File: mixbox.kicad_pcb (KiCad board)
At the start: 2 copper layers, 98.9 x 53.4 mm, 24 parts, among them J1 Conn_01x05_Male, J2 Conn_01x06_Male, SW1 SW_Push, SW2 SW_Push, SW3 SW_Push, SW4 SW_Push, SW5 SW_Push, SW6 SW_Push, SW7 SW_Push, SW8 SW_Push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

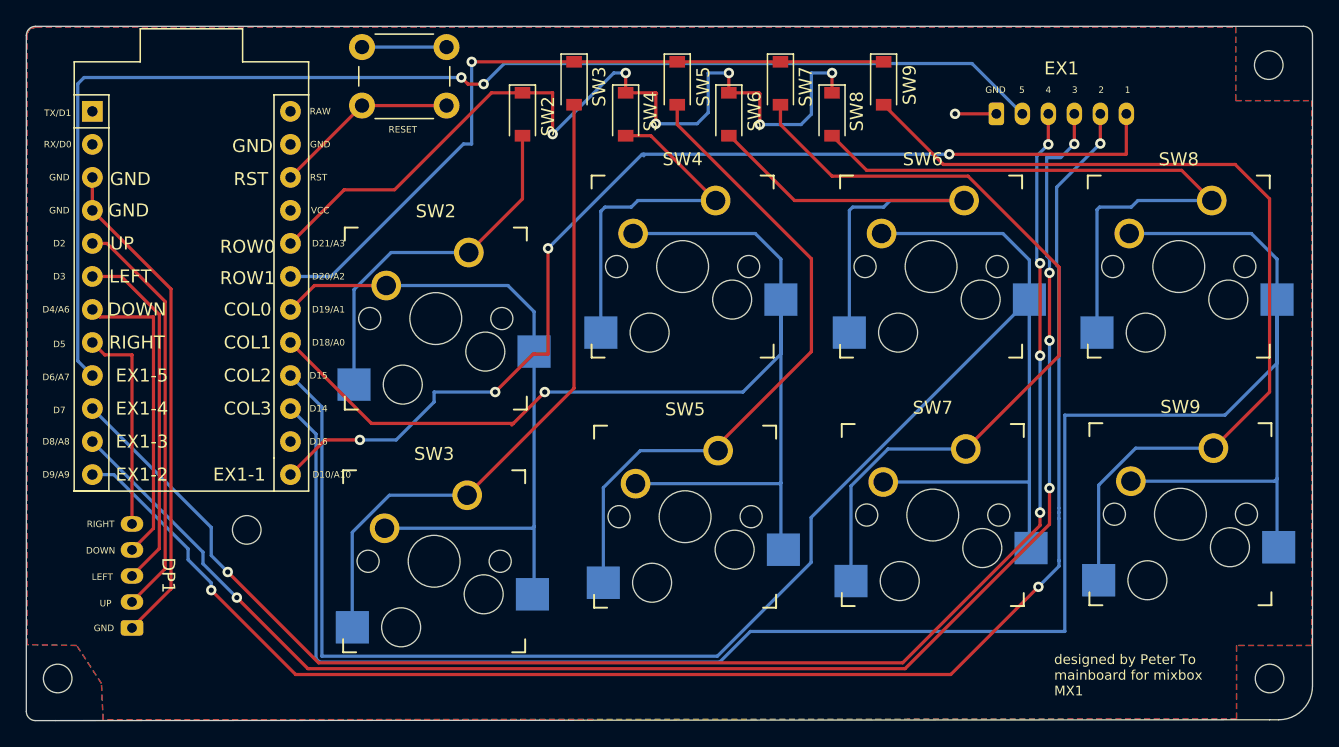
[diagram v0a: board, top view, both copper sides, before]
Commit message: Updates rows and columns in pcbnew and updates J2 from 1x06 to 1x05 connector
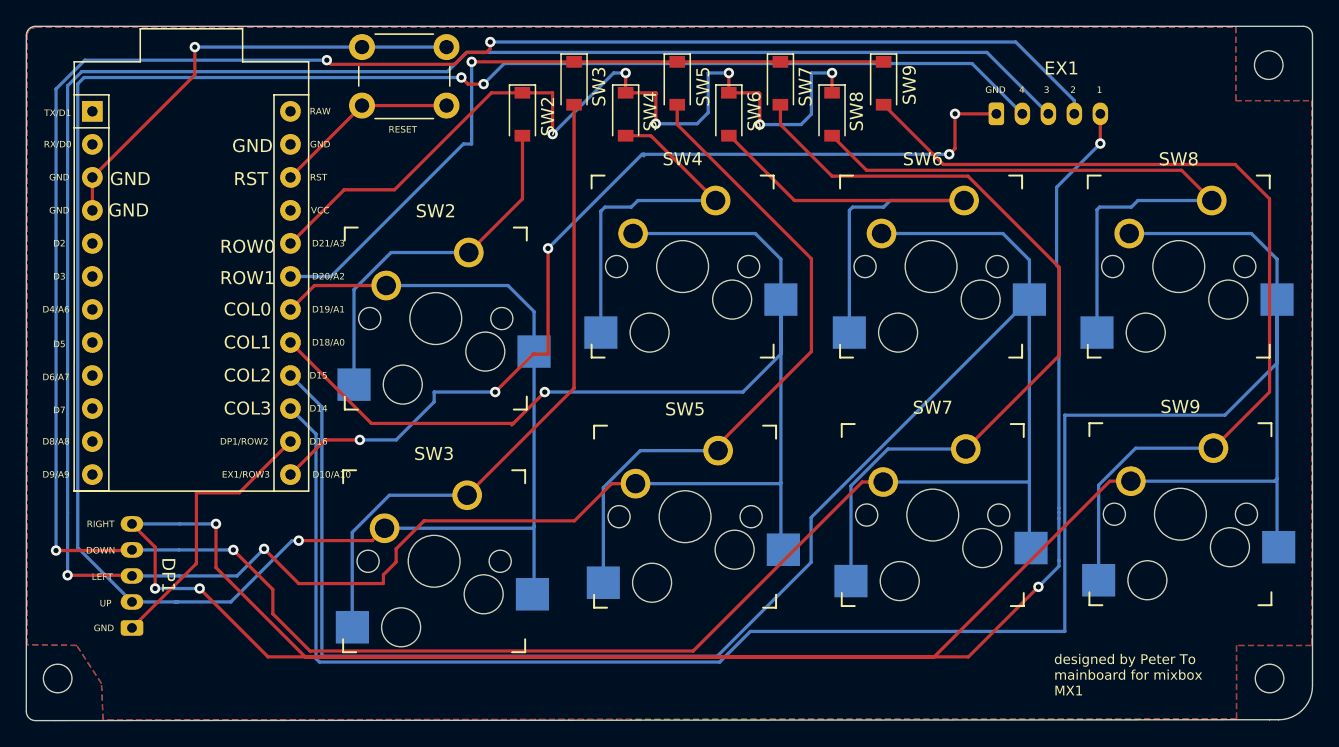
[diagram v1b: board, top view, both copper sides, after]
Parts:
- removed the REF** at (155.0, 104.2)
- J2: value Conn_01x06_Male -> Conn_01x05_Male; footprint Connector_JST:JST_PH_S6B-PH-K_1x06_P2.00mm_Horizontal -> Connector_JST:JST_PH_S5B-PH-K_1x05_P2.00mm_Horizontal
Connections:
- J1 pad 1: GND -> Net-(J1-Pad1)
- J1 pad 2: Net-(J1-Pad2) -> COL0
- J1 pad 3: Net-(J1-Pad3) -> COL1
- J1 pad 4: Net-(J1-Pad4) -> COL2
- J1 pad 5: Net-(J1-Pad5) -> COL3
- J2 pad 1: GND -> Net-(J2-Pad1)
- J2 pad 2: Net-(J2-Pad2) -> COL0
- J2 pad 3: Net-(J2-Pad3) -> COL1
- J2 pad 4: Net-(J2-Pad4) -> COL2
- J2 pad 5: Net-(J2-Pad5) -> COL3
- U1 pad 10: Net-(J2-Pad3) -> Net-(U1-Pad10)
- U1 pad 11: Net-(J2-Pad4) -> Net-(U1-Pad11)
- U1 pad 12: Net-(J2-Pad5) -> Net-(U1-Pad12)
- U1 pad 13: Net-(J2-Pad6) -> Net-(J2-Pad1)
- U1 pad 14: Net-(U1-Pad14) -> Net-(J1-Pad1)
- U1 pad 5: Net-(J1-Pad2) -> Net-(U1-Pad5)
- U1 pad 6: Net-(J1-Pad3) -> Net-(U1-Pad6)
- U1 pad 7: Net-(J1-Pad4) -> Net-(U1-Pad7)
- U1 pad 8: Net-(J1-Pad5) -> Net-(U1-Pad8)
- U1 pad 9: Net-(J2-Pad2) -> Net-(U1-Pad9)
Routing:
- net COL3: track 164.0 -> 369.3 mm, vias 0 -> 5
- net COL2: track 139.9 -> 332.2 mm, vias 0 -> 4
- net COL1: track 92.7 -> 258.6 mm, vias 1 -> 3
- net COL0: track 53.8 -> 192.7 mm, vias 0 -> 3
- net Net-(J2-Pad5): track 121.3 -> 0.00 mm, vias 3 -> 0
- net Net-(J2-Pad4): track 119.2 -> 0.00 mm, vias 5 -> 0
- net Net-(J2-Pad3): track 118.8 -> 0.00 mm, vias 5 -> 0
- net Net-(J2-Pad2): track 98.2 -> 0.00 mm, vias 2 -> 0
- net Net-(J2-Pad6): track 82.9 -> 0.00 mm, vias 4 -> 0
- net Net-(J2-Pad1): track 0.00 -> 72.7 mm, vias 0 -> 5
- net Net-(J1-Pad2): track 31.6 -> 0.00 mm
- net Net-(J1-Pad3): track 27.3 -> 0.00 mm
- net Net-(J1-Pad4): track 23.5 -> 0.00 mm
- net Net-(J1-Pad1): track 0.00 -> 21.3 mm
- net Net-(J1-Pad5): track 16.4 -> 0.00 mm
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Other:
- board text added: "DP1/ROW2"
- board text added: "EX1/ROW3"
- board text removed: "5"
- board text removed: "EX1-1"
- board text removed: "EX1-2"
- board text removed: "EX1-3"
- board text removed: "EX1-4"
- board text removed: "EX1-5"

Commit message: Updates columns to terminate at the J2 end instead of the first row of the face buttons
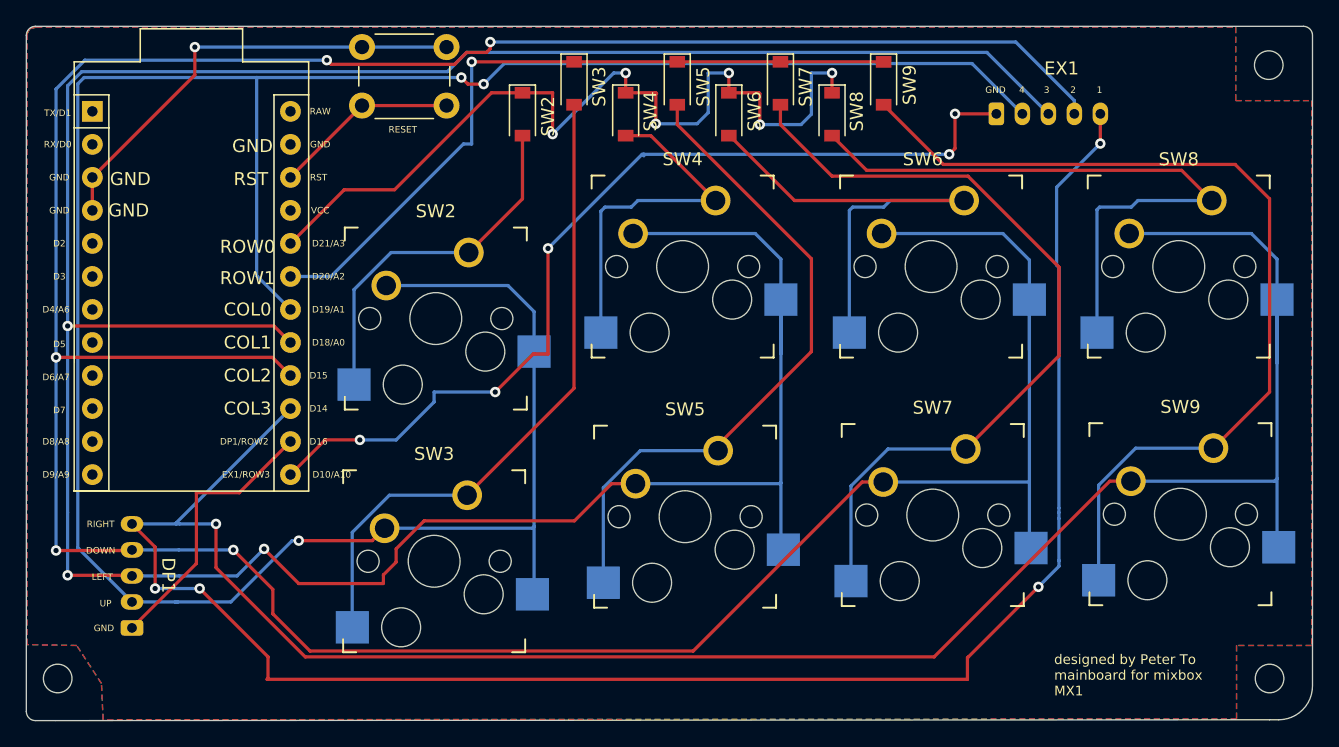
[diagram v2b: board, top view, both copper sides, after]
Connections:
- net Net-(D1-Pad1) renamed ROW0
- net Net-(D2-Pad1) renamed ROW1
- net Net-(J1-Pad1) renamed ROW2
- net Net-(J2-Pad1) renamed ROW3
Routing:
- net COL3: track 369.3 -> 272.0 mm
- net COL2: track 332.2 -> 260.4 mm, vias 4 -> 5
- net COL1: track 258.6 -> 233.6 mm
- net COL0: track 192.7 -> 203.5 mm
